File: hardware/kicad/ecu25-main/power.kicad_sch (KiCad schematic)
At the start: 25 parts, among them J1 Screw_Terminal_BATT, Q1 SQD50P06-15L, U1 LM5164DDA-Q1, U2 TLV75533 (500mA)

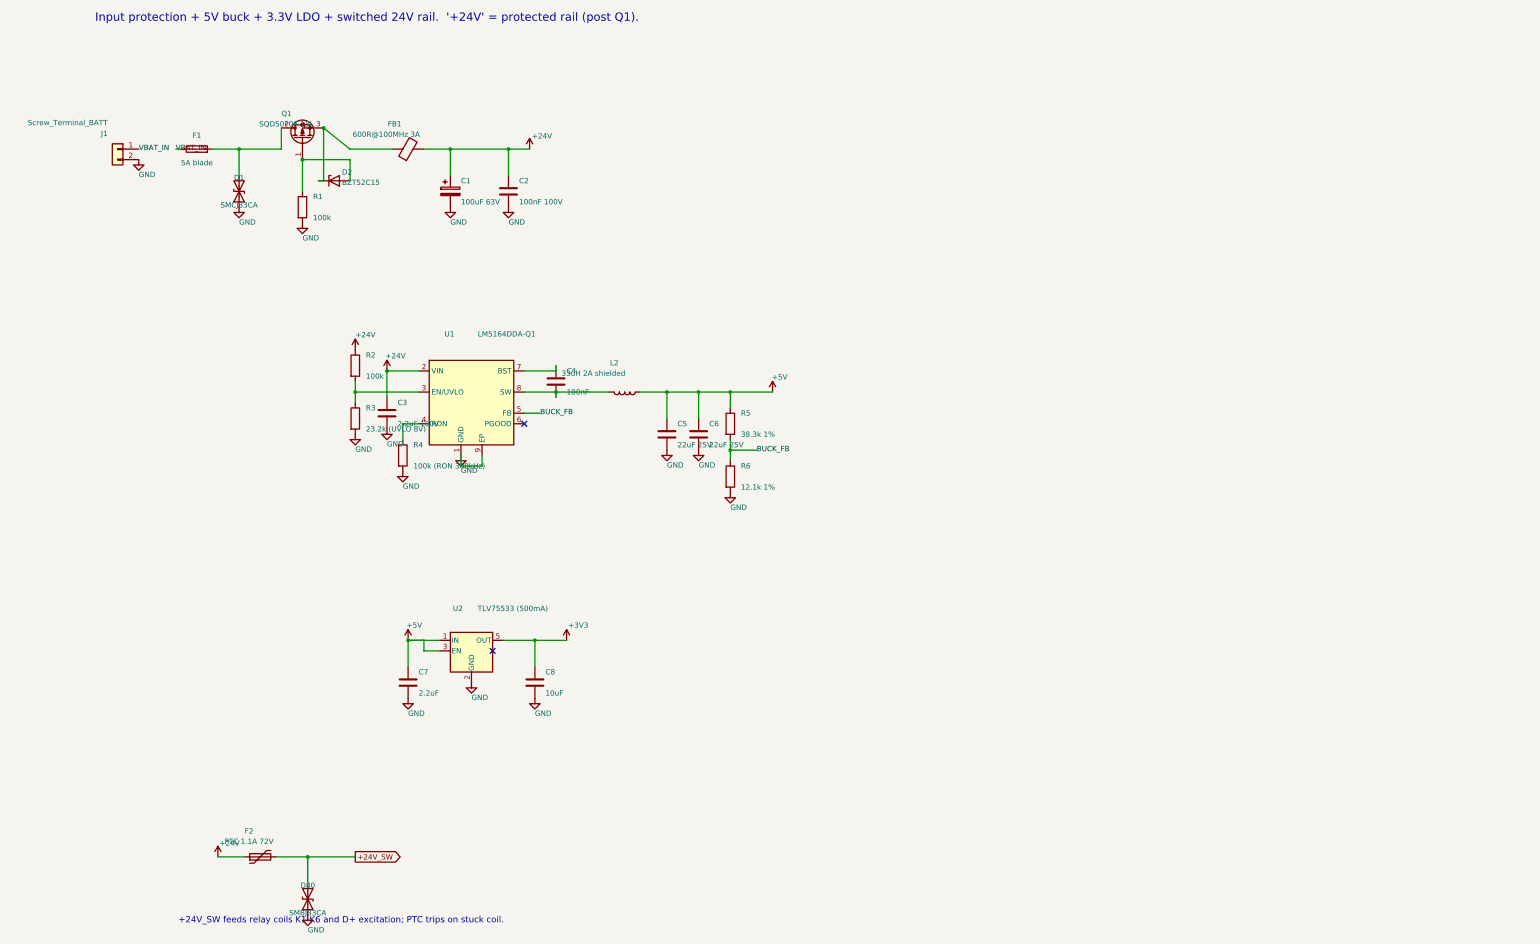
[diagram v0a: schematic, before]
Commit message: Convert hardware to 12 V system; pilot-duty output stage
The target set is a Kirloskar KG4-25WS1 (engine 3R550ETA 4G1, CPCB IV+):
12 V electrical system, 75 Ah battery, 3-cylinder CRDi with EGR + DOC.
The board was designed 24 V throughout, which was wrong.

Power:
- Rails renamed +24V/+24V_SW -> +12V/+12V_SW
- Buck UVLO 8.0 V -> 6.5 V (R3 30.1k), RON 100k -> 49.9k to hold ~300 kHz
  from a 12 V input
- New D3 blocking Schottky + C9 2200uF hold-up on the buck input. UVLO now
  senses the hold-up node, not the battery: sensing the battery would trip EN
  the moment the harness sagged during crank and switch the buck off while C9
  still held charge. Sized for >50 ms down to 6.5 V with the backlight shed
- Input protection rescaled for 12 V: D1 SMCJ33CA -> SMCJ16CA (clamps ~26 V
  not 53 V), D80 -> SMBJ16CA, D2 gate zener 15 V -> 12 V, C1 63 V -> 35 V

Outputs — the board no longer sources any field current:
- J8 becomes a 6-pole body with 5 poles wired: pin 1 OUT_COM is the common
  contact supply, fed by the INSTALLER from a fused source. Relay contact COMs
  come from it, not from the board rail
- +12V_SW now feeds only the six relay coils (200 mA) and D+ (100 mA)
- START marked pilot-only: a 12 V starter solenoid pulls 20-40 A and glow
  plugs 28-60 A, against 8 A DC contacts
- K5/K6 HORN/PREHEAT -> configurable AUX1/AUX2; on a CRDi engine the ECU owns
  the cold-start aid, so a fixed preheat channel would often go unused
- Relay coils G5LE-1-DC24 -> DC12 (360 ohm / 33 mA)

Analog rescaled for 12 V:
- DIN dividers 10k/3.3k -> 5.6k/1.8k, restoring 1.6 mA contact wetting
  (10k/3.3k gives only 0.9 mA at 12 V), debounce cap 470 nF -> 1 uF
- Battery and D+ sense 100k/6.8k -> 100k/22k, so 16 V uses most of the ADC span
- D+ excitation 220R 5W -> 120R 3W for the same 100 mA at 12 V

Verified: netlist sweep clean, no courtyard overlaps, nothing outside the
outline, DRC reports no errors (unrouted ratsnest and silk warnings aside).
Docs and firmware follow in the next com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
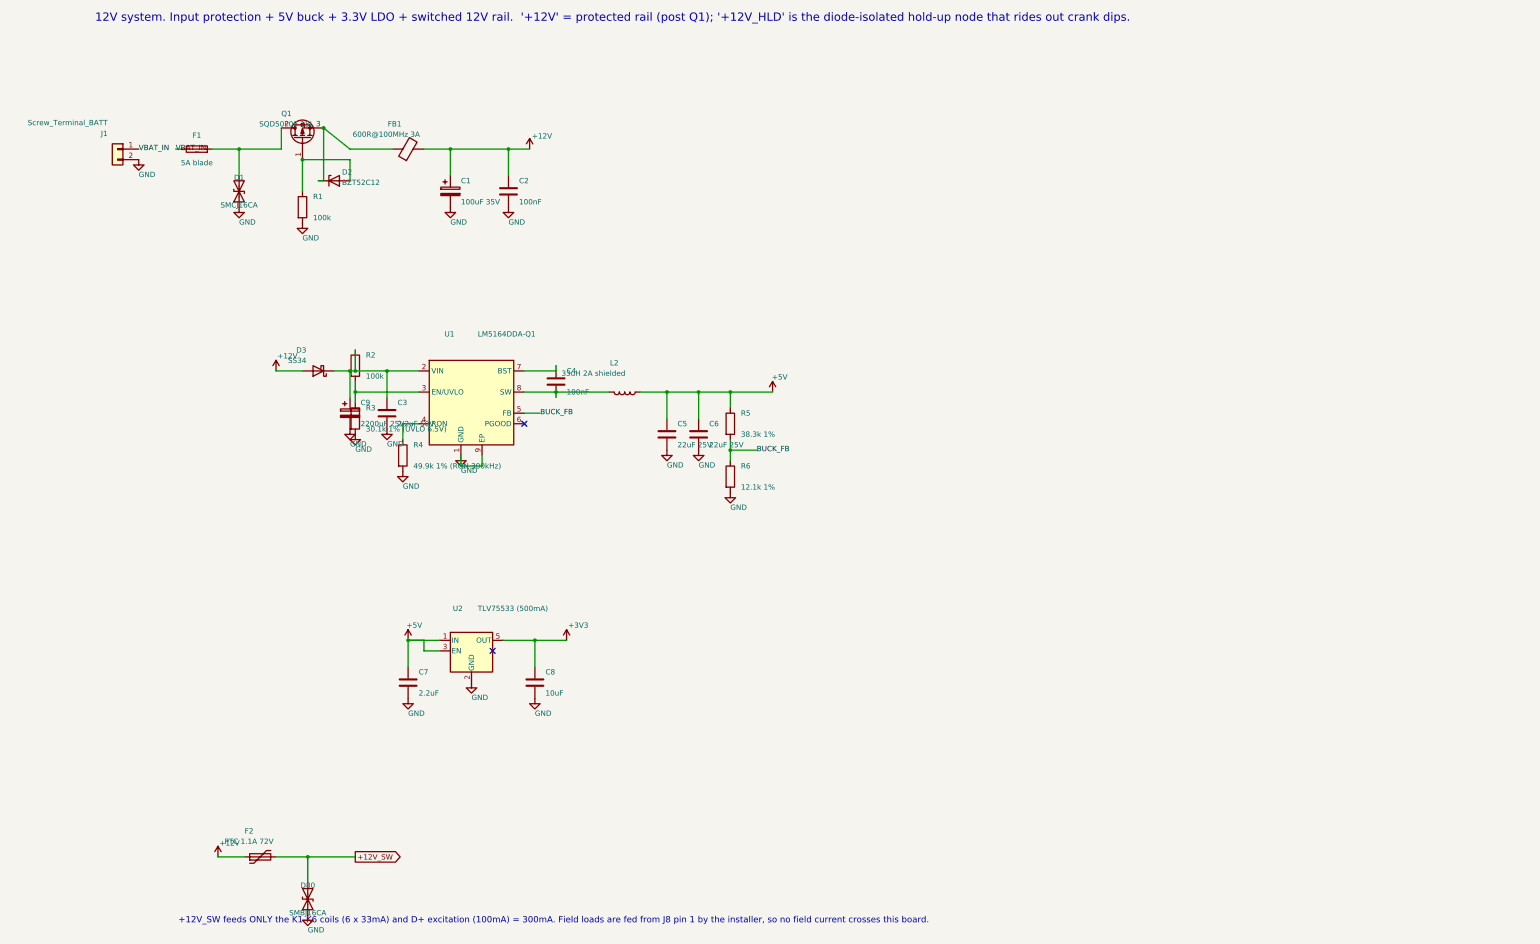
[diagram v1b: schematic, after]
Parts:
- added C9: 2200uF 25V, Capacitor_THT:CP_Radial_D12.5mm_P5.00mm, symbol Device:C_Polarized
- added D3: SS34, Diode_SMD:D_SMA, symbol Device:D_Schottky
- C1: value 100uF 63V -> 100uF 35V; footprint Capacitor_THT:CP_Radial_D10.0mm_P5.00mm -> Capacitor_THT:CP_Radial_D8.0mm_P3.50mm
- C2: value 100nF 100V -> 100nF; footprint Capacitor_SMD:C_0805_2012Metric -> Capacitor_SMD:C_0603_1608Metric
- C3: value 2.2uF 100V -> 2.2uF 50V
- D1: value SMCJ33CA -> SMCJ16CA
- D2: value BZT52C15 -> BZT52C12
- D80: value SMBJ33CA -> SMBJ16CA
- R3: value 23.2k (UVLO 8V) -> 30.1k 1% (UVLO 6.5V)
- R4: value 100k (RON 300kHz) -> 49.9k 1% (RON 300kHz)
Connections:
- net GND: now also C9.2
- net +24V renamed +12V
- net +12V: now also D3.2 (A); no longer C3.1, R2.1, U1.2 (VIN)
- net +24V_SW renamed +12V_SW
- new net: C3.1, C9.1, D3.1 (K), R2.1, U1.2 (VIN)
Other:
- note added: "+12V_SW feeds ONLY the K1-K6 coils (6 x 33mA) and D+ excitation (100mA) = 300mA. Field loads are fed from J8 pin 1 by the installer, so no field current crosses this board."
- note added: "12V system. Input protection + 5V buck + 3.3V LDO + switched 12V rail. '+12V' = protected rail (post Q1); '+12V_HLD' is the diode-isolated hold-up node that rides out crank dips."
- note removed: "+24V_SW feeds relay coils K1-K6 and D+ excitation; PTC trips on stuck coil."
- note removed: "Input protection + 5V buck + 3.3V LDO + switched 24V rail. '+24V' = protected rail (post Q1)."

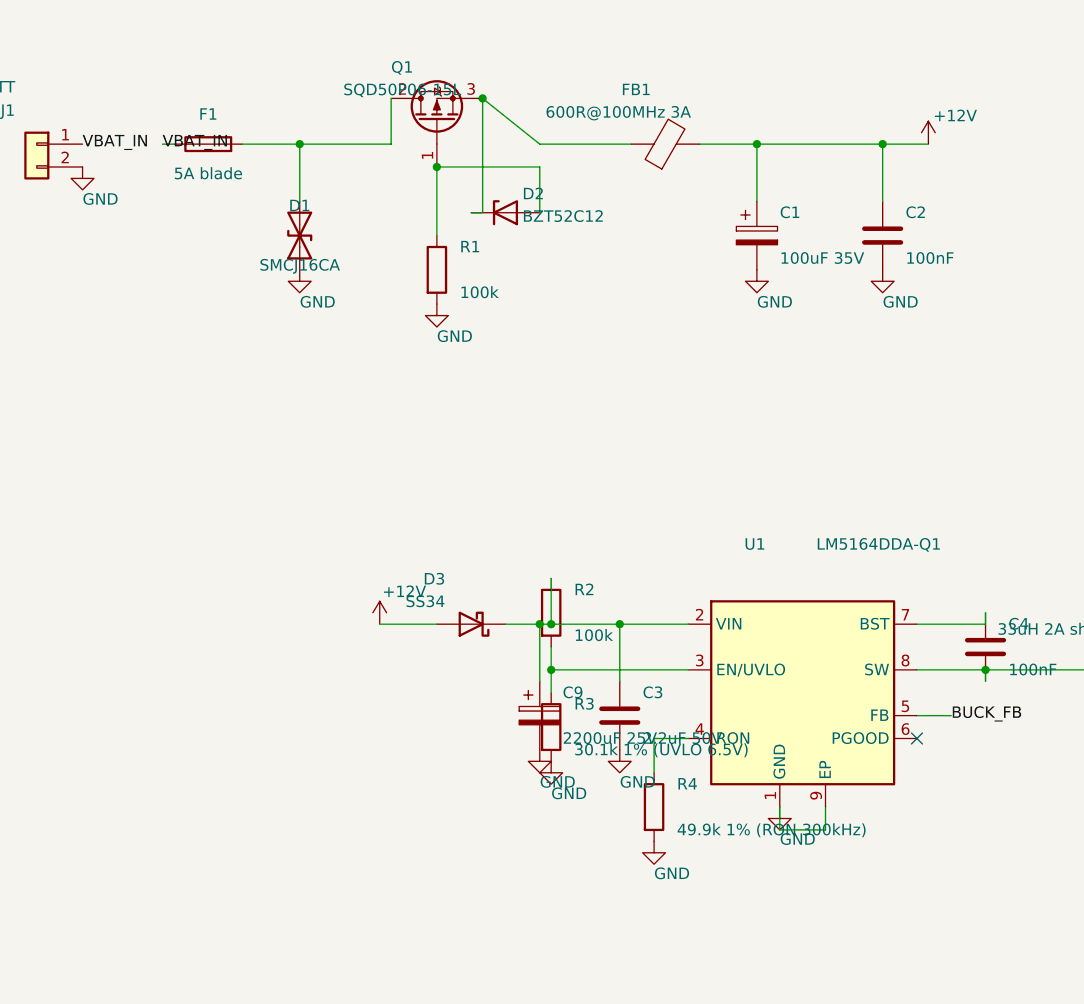
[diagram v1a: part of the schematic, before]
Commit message: Fix SME review findings on the 12 V conversion
Two criticals, both of which would have reached a real installation:

- gcu_config.c still carried 24 V battery thresholds (22 V low / 30 V high).
  On a 12 V set batt_low was permanently true, so 60 s after every power-up
  the alarm latched and pinned the horn relay on for good — while batt_high
  at 30 V could never trip, leaving a runaway regulator undetected exactly
  where the new 16 V TVS starts conducting. Now 11.0 / 15.5 V, with a
  regression test that runs 90 s at 13.8 V and asserts silence
- docs/ecu-25-explained.md still told the installer to wire the starter
  solenoid straight to K2 at '16 A'. A G5LE-1 is 8 A DC and a 12 V starter
  solenoid pulls 20-40 A: the contacts weld, and a welded starter contact
  means the engine cranks and cannot be commanded to stop. Section rewritten
  around the dry-contact stage

Majors:
- gen_pcb.py netclass patterns still named +24V/+24V_SW, so the battery rail,
  the switched rail, the hold-up node and OUT_COM all fell through to a
  0.25 mm Default track — OUT_COM being the common return for every field
  contact. Fixed, and the generator now fails if any netclass pattern matches
  no net, which is what would have caught it
- DIN ground-side pull-up 5.6k -> 2.2k: at 5.6k an open contact sat at 1.66 V,
  inside the STM32's indeterminate band (V_IL 1.12 / V_IH 1.79)
- Buck RON 49.9k -> 41.2k. The LM5164's f_SW = V_OUT x 2500 / R_RON has no
  V_IN term — on-time varies inversely with V_IN precisely so frequency stays
  constant — so the rationale in two documents was wrong, and the original
  100k was never 300 kHz at any input voltage, it was 125 kHz
- modbus_rx guarded resp_max >= 5 but the FC06/FC16 echo paths write 8 bytes,
  running three bytes past the caller's buffer. Guard raised to 8
- Modbus no longer publishes a fabricated power factor: registers 19/20 now
  carry real_power_w and power_factor from gcu_inputs_t, which the AC layer
  fills. A constant 0.800 in a S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
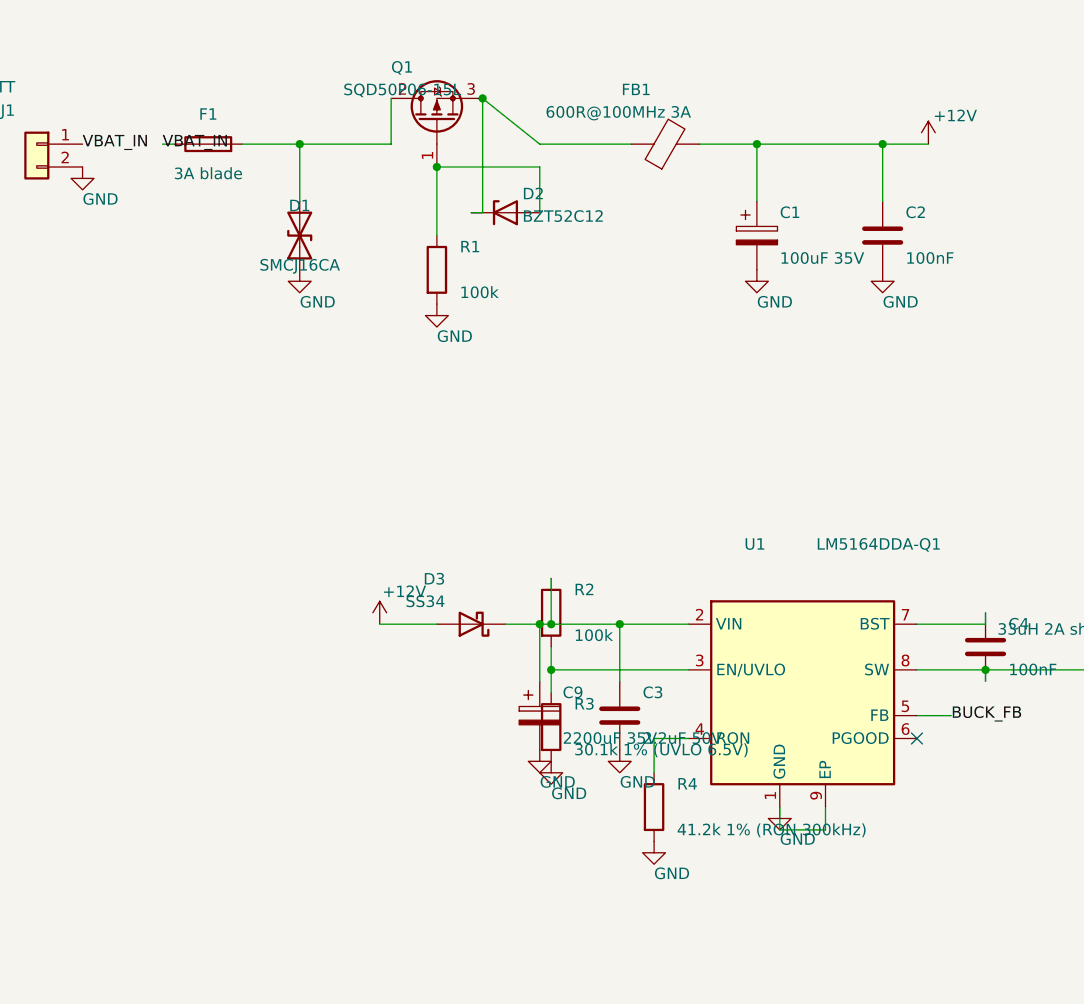
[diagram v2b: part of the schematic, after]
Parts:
- C9: value 2200uF 25V -> 2200uF 35V
- F1: value 5A blade -> 3A blade
- R4: value 49.9k 1% (RON 300kHz) -> 41.2k 1% (RON 300kHz)
